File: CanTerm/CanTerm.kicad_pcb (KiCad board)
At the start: 2 copper layers, 10 x 6.5 mm, 2 parts, among them J1 Conn_01x02

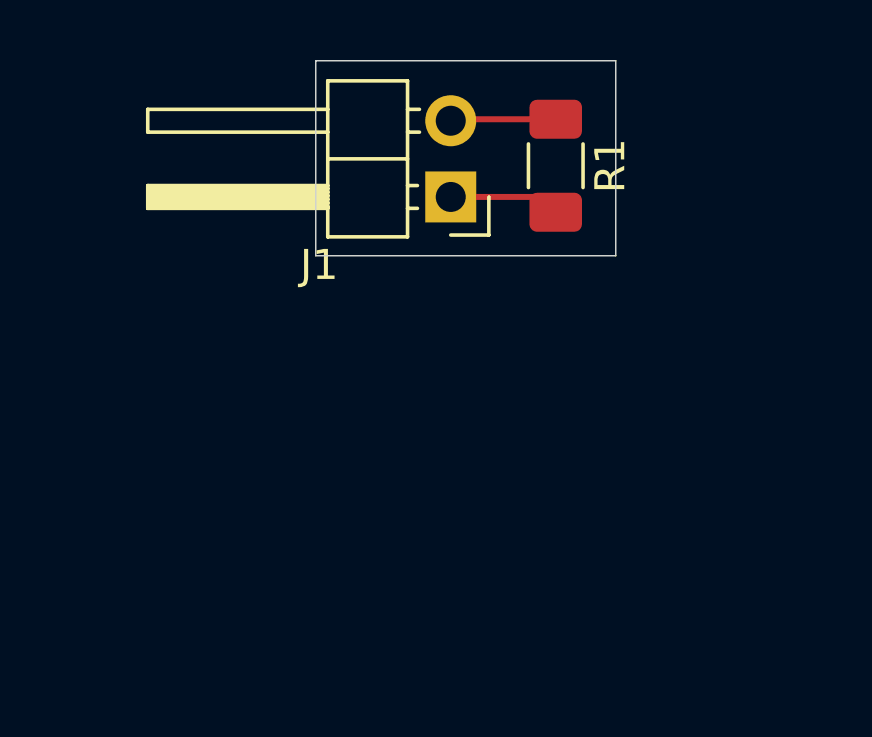
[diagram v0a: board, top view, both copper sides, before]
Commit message: Added molexSL footprint and improved CanTerm
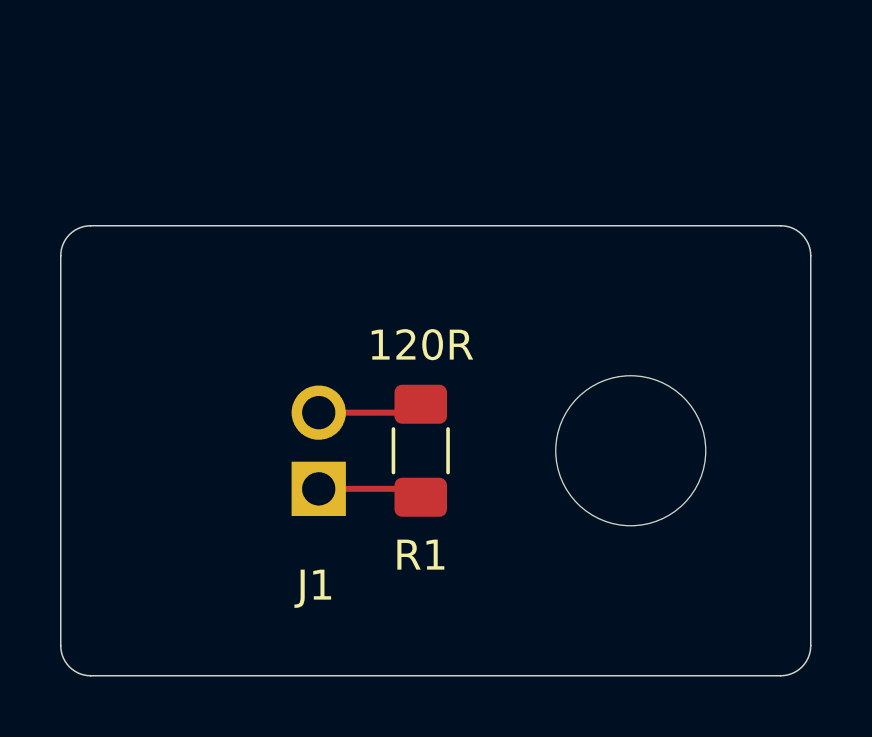
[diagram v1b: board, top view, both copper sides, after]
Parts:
- added H1: MountingHole, MountingHole:MountingHole_5mm, F.Cu at (136.5, 100.0)
- J1: footprint Connector_PinHeader_2.54mm:PinHeader_1x02_P2.54mm_Horizontal -> FRC5010-FootprintLibrary:Molex_SL_RightAngle_Through_1x02
- moved J1 13.5 mm to (120.0, 100.0), turned to 0 degrees
- moved R1 10.5 mm to (129.5, 100.0), turned to 90 degrees
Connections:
- R1 pad 1: Net-(J1-Pin_2) -> Net-(J1-Pin_1)
- R1 pad 2: Net-(J1-Pin_1) -> Net-(J1-Pin_2)
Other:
- board size 10 x 6.5 mm -> 25 x 15 mm
- board text added: "WayWayWay"
- board text added: "[TiDy] CanTerm 1.0"
